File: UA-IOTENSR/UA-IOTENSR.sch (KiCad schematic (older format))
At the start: 5 parts, among them IC101 LM3914VX_NOPB, SW101 SW_MEC_5G, U101 ESP32-S2-WROOM, U102 SCD4X

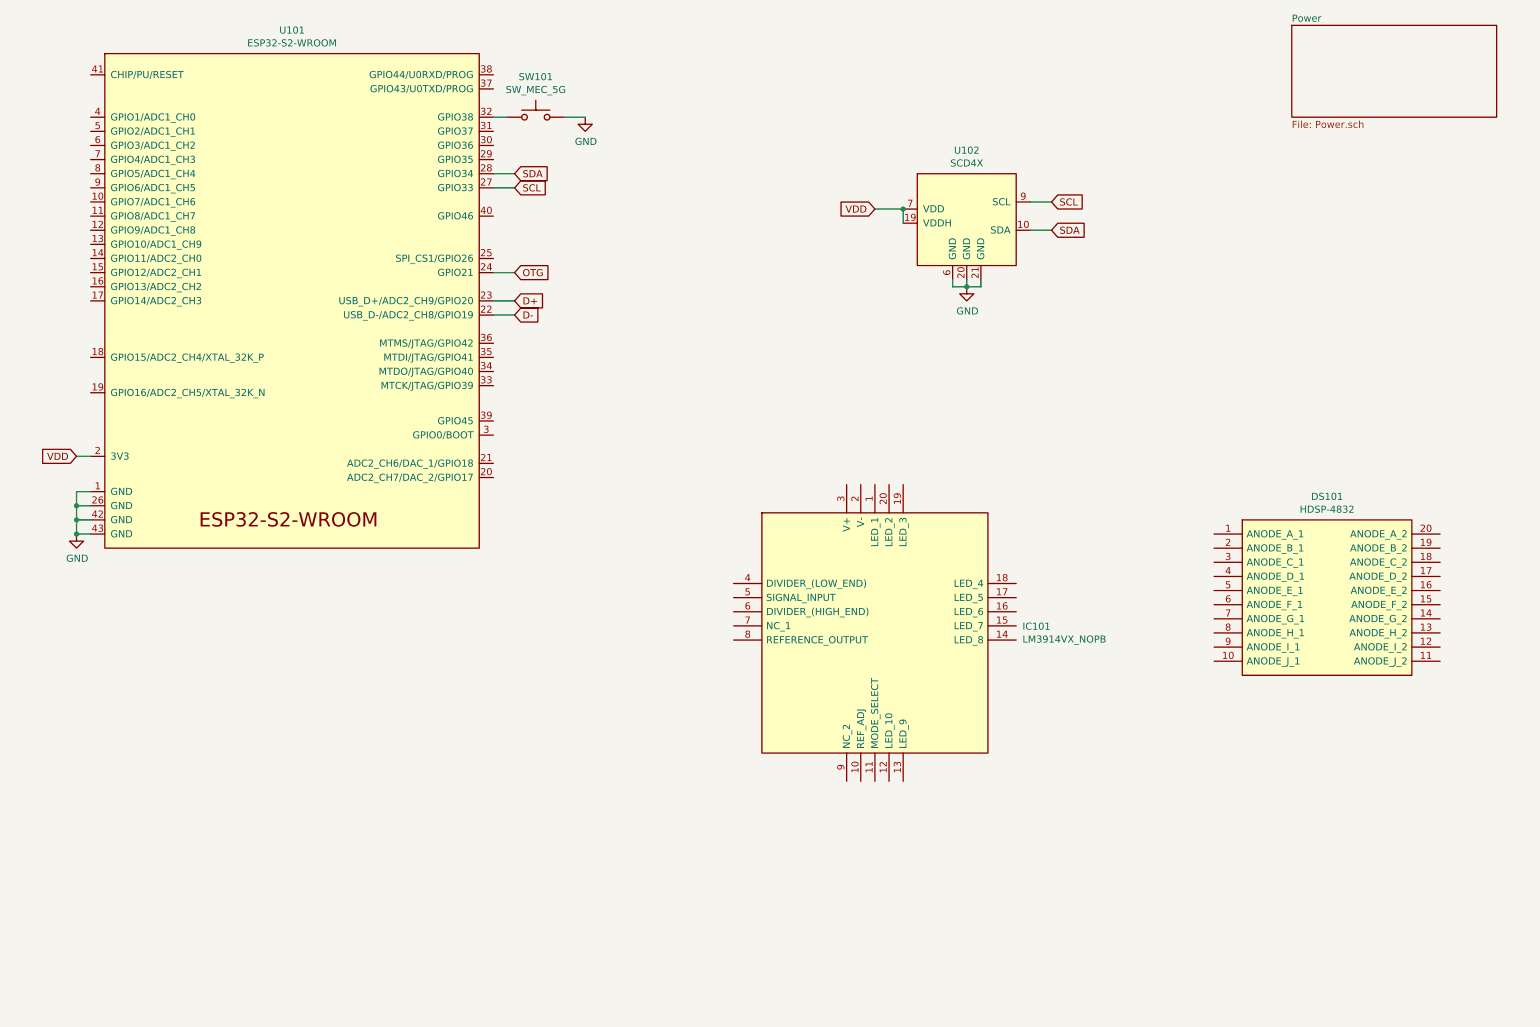
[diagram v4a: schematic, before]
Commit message: Adding peripherals page
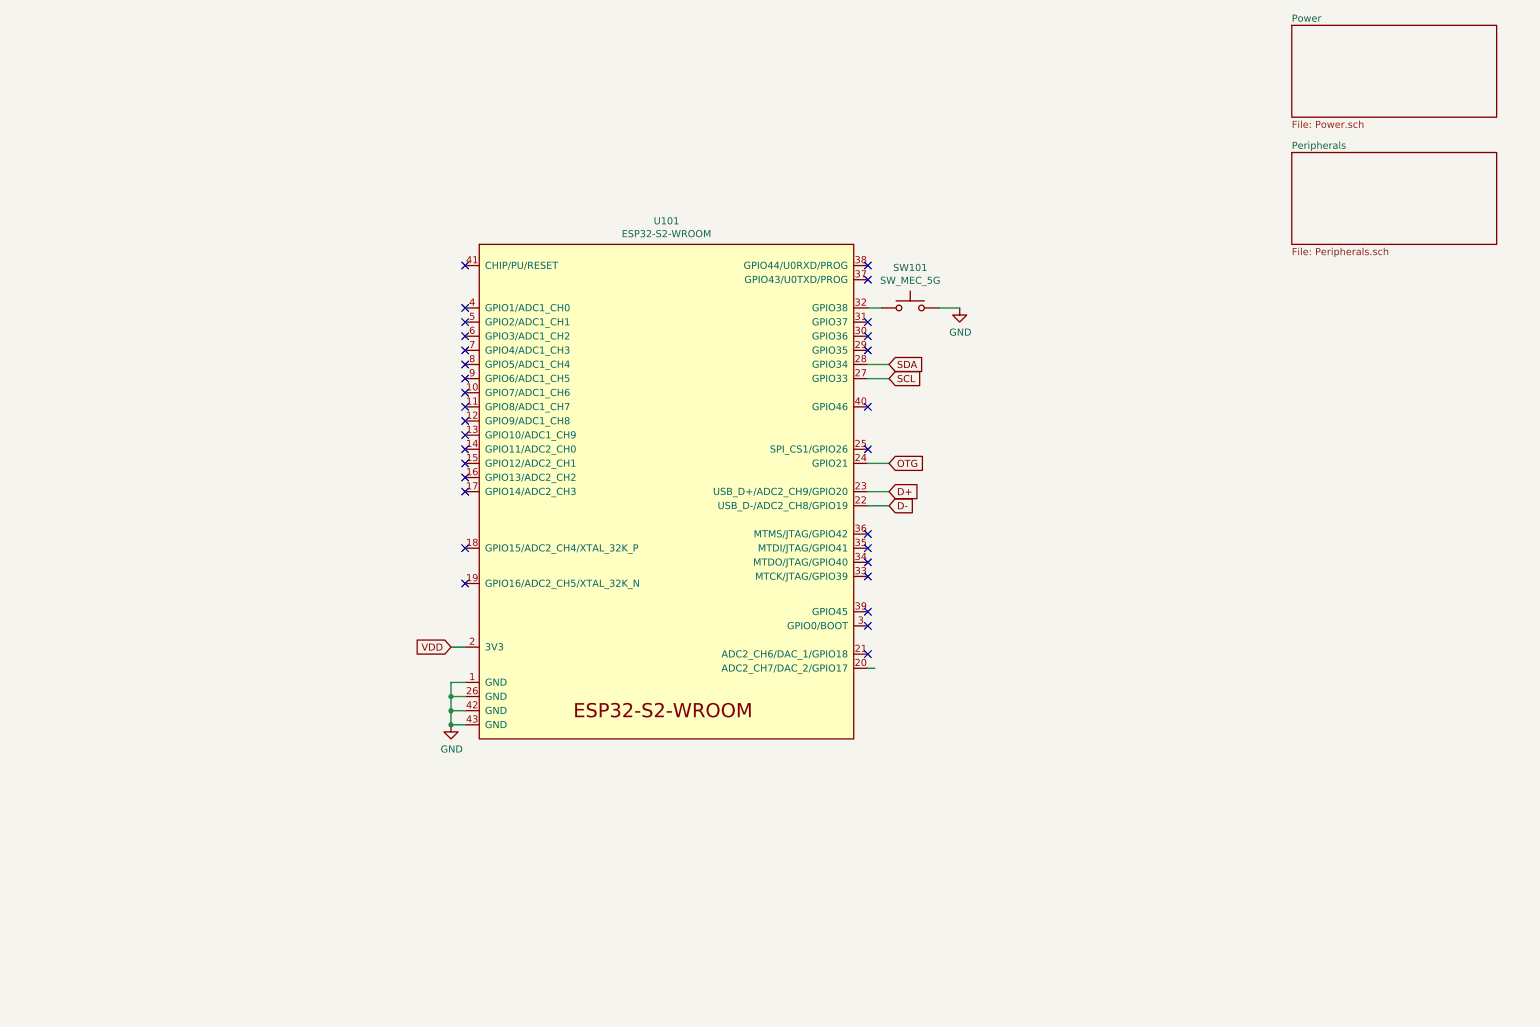
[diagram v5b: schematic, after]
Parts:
- removed DS101: HDSP-4832, DIPS762W61P254L2540H635Q20N, symbol Samacs:HDSP-4832
- removed IC101: LM3914VX_NOPB, PLCC127P990X990X457-20N, symbol Samacs:LM3914VX_NOPB
- removed U102: SCD4X, symbol SCD4X:SCD4X
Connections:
- wire segments 24 -> 16
- no-connect marks 0 -> 31
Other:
- moved on the sheet: SW101, U101
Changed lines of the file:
@@
 $Descr A4 11693 8268
 encoding utf-8
-Sheet 1 2
+Sheet 1 3
 Title ""
 Date ""
@@
 $EndDescr
 $Comp
-L SCD4X:SCD4X U102
-U 1 1 6195D75D
-P 7300 1950
-F 0 "U102" H 7300 2415 50  0000 C CNN
-F 1 "SCD4X" H 7300 2324 50  0000 C CNN
-F 2 "" H 7300 2400 50  0001 C CNN
-F 3 "" H 7300 2400 50  0001 C CNN
-	1    7300 1950
+L power:GND #PWR0101
+U 1 1 61961638
+P 3650 5550
+F 0 "#PWR0101" H 3650 5300 50  0001 C CNN
+F 1 "GND" H 3655 5377 50  0000 C CNN
+F 2 "" H 3650 5550 50  0001 C CNN
+F 3 "" H 3650 5550 50  0001 C CNN
+	1    3650 5550
 	1    0    0    -1
 $EndComp
 Wire Wire Line
-	7750 1850 7900 1850
+	3650 5350 3750 5350
 Wire Wire Line
-	7750 2050 7900 2050
-Text GLabel 7900 1850 2    50   Input ~ 0
-SCL
-Text GLabel 7900 2050 2    50   Input ~ 0
-SDA
+	3650 5450 3750 5450
+Wire Wire Line
+	3650 5550 3750 5550
 $Comp
-L power:GND #PWR0101
-U 1 1 61961638
-P 1000 4200
-F 0 "#PWR0101" H 1000 3950 50  0001 C CNN
-F 1 "GND" H 1005 4027 50  0000 C CNN
-F 2 "" H 1000 4200 50  0001 C CNN
-F 3 "" H 1000 4200 50  0001 C CNN
-	1    1000 4200
+L Espressif:ESP32-S2-WROOM U101
+U 1 1 619E5D94
+P 5150 3900
+F 0 "U101" H 5175 5815 50  0000 C CNN
+F 1 "ESP32-S2-WROOM" H 5175 5724 50  0000 C CNN
+F 2 "Espressif:ESP32-S2-WROOM" H 5150 2000 50  0001 C CNN
+F 3 "https://www.espressif.com/sites/default/files/documentation/esp32-s2-wroom_esp32-s2-wroom-i_datasheet_en.pdf" H 5150 3900 50  0001 C CNN
+	1    5150 3900
 	1    0    0    -1
 $EndComp
 Wire Wire Line
-	7200 2400 7200 2450
+	3750 5250 3650 5250
 Wire Wire Line
-	7200 2450 7300 2450
+	3650 5250 3650 5350
+Connection ~ 3650 5350
 Wire Wire Line
-	7400 2450 7400 2400
+	3650 5350 3650 5450
+Connection ~ 3650 5450
 Wire Wire Line
-	7300 2400 7300 2450
-Connection ~ 7300 2450
+	3650 5450 3650 5550
+Connection ~ 3650 5550
 Wire Wire Line
-	7300 2450 7400 2450
+	6600 3100 6750 3100
+Text GLabel 6750 3100 2    50   Input ~ 0
+SCL
+Text GLabel 6750 3000 2    50   Input ~ 0
+SDA
+Wire Wire Line
+	6600 3000 6750 3000
+Wire Wire Line
+	7100 2600 7250 2600
 $Comp
-L power:GND #PWR0104
-U 1 1 61967846
-P 7300 2450
-F 0 "#PWR0104" H 7300 2200 50  0001 C CNN
-F 1 "GND" H 7305 2277 50  0000 C CNN
-F 2 "" H 7300 2450 50  0001 C CNN
-F 3 "" H 7300 2450 50  0001 C CNN
-	1    7300 2450
+L Switch:SW_MEC_5G SW101
+U 1 1 619D98CD
+P 6900 2600
+F 0 "SW101" H 6900 2885 50  0000 C CNN
+F 1 "SW_MEC_5G" H 6900 2794 50  0000 C CNN
+F 2 "" H 6900 2800 50  0001 C CNN
+F 3 "http://www.apem.com/int/index.php?controller=attachment&id_attachment=488" H 6900 2800 50  0001 C CNN
+	1    6900 2600
 	1    0    0    -1
 $EndComp
 Wire Wire Line
-	1000 4000 1100 4000
-Wire Wire Line
-	1000 4100 1100 4100
-Wire Wire Line
-	1000 4200 1100 4200
+	6600 2600 6700 2600
 $Comp
-L Espressif:ESP32-S2-WROOM U101
-U 1 1 619E5D94
-P 2500 2550
-F 0 "U101" H 2525 4465 50  0000 C CNN
-F 1 "ESP32-S2-WROOM" H 2525 4374 50  0000 C CNN
-F 2 "Espressif:ESP32-S2-WROOM" H 2500 650 50  0001 C CNN
-F 3 "https://www.espressif.com/sites/default/files/documentation/esp32-s2-wroom_esp32-s2-wroom-i_datasheet_en.pdf" H 2500 2550 50  0001 C CNN
-	1    2500 2550
+L power:GND #PWR0102
+U 1 1 61A04BEB
+P 7250 2600
+F 0 "#PWR0102" H 7250 2350 50  0001 C CNN
+F 1 "GND" H 7255 2427 50  0000 C CNN
+F 2 "" H 7250 2600 50  0001 C CNN
+F 3 "" H 7250 2600 50  0001 C CNN
+	1    7250 2600
 	1    0    0    -1
 $EndComp
 Wire Wire Line
-	1100 3900 1000 3900
-Wire Wire Line
-	1000 3900 1000 4000
-Connection ~ 1000 4000
-Wire Wire Line
-	1000 4000 1000 4100
-Connection ~ 1000 4100
-Wire Wire Line
-	1000 4100 1000 4200
-Connection ~ 1000 4200
-Wire Wire Line
-	3950 1750 4100 1750
-Text GLabel 4100 1750 2    50   Input ~ 0
-SCL
-Text GLabel 4100 1650 2    50   Input ~ 0
-SDA
-Wire Wire Line
-	3950 1650 4100 1650
-Wire Wire Line
-	4450 1250 4600 1250
-$Comp
-L Switch:SW_MEC_5G SW101
-U 1 1 619D98CD
-P 4250 1250
-F 0 "SW101" H 4250 1535 50  0000 C CNN
-F 1 "SW_MEC_5G" H 4250 1444 50  0000 C CNN
-F 2 "" H 4250 1450 50  0001 C CNN
-F 3 "http://www.apem.com/int/index.php?controller=attachment&id_attachment=488" H 4250 1450 50  0001 C CNN
-	1    4250 1250
-	1    0    0    -1
-$EndComp
-Wire Wire Line
-	3950 1250 4050 1250
-$Comp
-L power:GND #PWR0102
-U 1 1 61A04BEB
-P 4600 1250
-F 0 "#PWR0102" H 4600 1000 50  0001 C CNN
-F 1 "GND" H 4605 1077 50  0000 C CNN
-F 2 "" H 4600 1250 50  0001 C CNN
-F 3 "" H 4600 1250 50  0001 C CNN
-	1    4600 1250
-	1    0    0    -1
-$EndComp
-Wire Wire Line
-	1100 3650 1000 3650
-Text GLabel 1000 3650 0    50   Input ~ 0
+	3750 5000 3650 5000
+Text GLabel 3650 5000 0    50   Input ~ 0
 VDD
-Wire Wire Line
-	6850 1900 6650 1900
-Text GLabel 6650 1900 0    50   Input ~ 0
-VDD
-Text GLabel 4100 2550 2    50   Input ~ 0
+Text GLabel 6750 3900 2    50   Input ~ 0
 D+
 Wire Wire Line
-	3950 2550 4100 2550
-Text GLabel 4100 2650 2    50   Input ~ 0
+	6600 3900 6750 3900
+Text GLabel 6750 4000 2    50   Input ~ 0
 D-
 Wire Wire Line
-	3950 2650 4100 2650
+	6600 4000 6750 4000
 Wire Wire Line
-	6850 2000 6850 1900
-Connection ~ 6850 1900
-Wire Wire Line
-	3950 2350 4100 2350
-Text GLabel 4100 2350 2    50   Input ~ 0
+	6600 3700 6750 3700
+Text GLabel 6750 3700 2    50   Input ~ 0
 OTG
-$Comp
-L Samacs:HDSP-4832 DS101
-U 1 1 619CEE0B
-P 9050 4200
-F 0 "DS101" H 9850 4465 50  0000 C CNN
-F 1 "HDSP-4832" H 9850 4374 50  0000 C CNN
-F 2 "DIPS762W61P254L2540H635Q20N" H 10500 4300 50  0001 L CNN
-F 3 "https://datasheet.datasheetarchive.com/originals/distributors/Datasheets-6/DSA-115790.pdf" H 10500 4200 50  0001 L CNN
-F 4 "Avago Light Bar Array Green/Red/Yellow LED Display, 1900 (Green) ??cd, 1900 (Yellow) ??cd, 3500 (Red) ??cd" H 10500 4100 50  0001 L CNN "Description"
-F 5 "6.35" H 10500 4000 50  0001 L CNN "Height"
-F 6 "630-HDSP-4832" H 10500 3900 50  0001 L CNN "Mouser Part Number"
-F 7 "https://www.mouser.co.uk/ProductDetail/Broadcom-Avago/HDSP-4832?qs=pQfy5%252BKCabLkjNEFwaYNQw%3D%3D" H 10500 3800 50  0001 L CNN "Mouser Price/Stock"
-F 8 "Avago Technologies" H 10500 3700 50  0001 L CNN "Manufacturer_Name"
-F 9 "HDSP-4832" H 10500 3600 50  0001 L CNN "Manufacturer_Part_Number"
-	1    9050 4200
-	1    0    0    -1
-$EndComp
-$Comp
-L Samacs:LM3914VX_NOPB IC101
-U 1 1 619D4939
-P 5650 4550
-F 0 "IC101" H 7694 4246 50  0000 L CNN
-F 1 "LM3914VX_NOPB" H 7694 4155 50  0000 L CNN
-F 2 "PLCC127P990X990X457-20N" H 7500 5050 50  0001 L CNN
-F 3 "http://www.ti.com/lit/gpn/lm3914" H 7500 4950 50  0001 L CNN
-F 4 "Dot/Bar Display Driver" H 7500 4850 50  0001 L CNN "Description"
-F 5 "4.57" H 7500 4750 50  0001 L CNN "Height"
-F 6 "926-LM3914VX/NOPB" H 7500 4650 50  0001 L CNN "Mouser Part Number"
-F 7 "https://www.mouser.co.uk/ProductDetail/Texas-Instruments/LM3914VX-NOPB?qs=QbsRYf82W3FGYq5LQoAqbA%3D%3D" H 7500 4550 50  0001 L CNN "Mouser Price/Stock"
-F 8 "Texas Instruments" H 7500 4450 50  0001 L CNN "Manufacturer_Name"
-F 9 "LM3914VX/NOPB" H 7500 4350 50  0001 L CNN "Manufacturer_Part_Number"
-	1    5650 4550
-	1    0    0    -1
-$EndComp
 $Sheet
 S 9600 600  1450 650
@@
 F1 "Power.sch" 50
 $EndSheet
+NoConn ~ 6600 5050
+NoConn ~ 6600 4850
+NoConn ~ 6600 4750
+NoConn ~ 6600 4500
+NoConn ~ 6600 4400
+NoConn ~ 6600 4300
+NoConn ~ 6600 4200
+NoConn ~ 6600 3600
+NoConn ~ 6600 3300
+NoConn ~ 6600 2900
+NoConn ~ 6600 2800
+NoConn ~ 6600 2700
+NoConn ~ 6600 2400
+NoConn ~ 6600 2300
+NoConn ~ 3750 2300
+NoConn ~ 3750 2600
+NoConn ~ 3750 2700
+NoConn ~ 3750 2800
+NoConn ~ 3750 2900
+NoConn ~ 3750 3000
+NoConn ~ 3750 3100
+NoConn ~ 3750 3200
+NoConn ~ 3750 3300
+NoConn ~ 3750 3400
+NoConn ~ 3750 3500
+NoConn ~ 3750 3600
+NoConn ~ 3750 3700
+NoConn ~ 3750 3800
+NoConn ~ 3750 3900
+NoConn ~ 3750 4300
+NoConn ~ 3750 4550
+Wire Wire Line
+	6600 5150 6650 5150
+$Sheet
+S 9600 1500 1450 650
+U 61A1DC3C
+F0 "Peripherals" 50
+F1 "Peripherals.sch" 50
+$EndSheet
 $EndSCHEMATC
